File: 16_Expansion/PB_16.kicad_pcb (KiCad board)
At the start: 2 copper layers, 139.5 x 71 mm, 56 parts, among them J1 String1, J10 String10, J11 String11, J12 String12, J13 String13, J14 String14, J15 String15, J16 String16, J17 Power In Left, J18 Power In Right, J19 Expansion Header, J2 String2, J3 String3, J4 String4, J5 String5, J6 String6, J7 String7, J8 String8, J9 String9, U1 SN74HCT245N, U2 SN74HCT245N

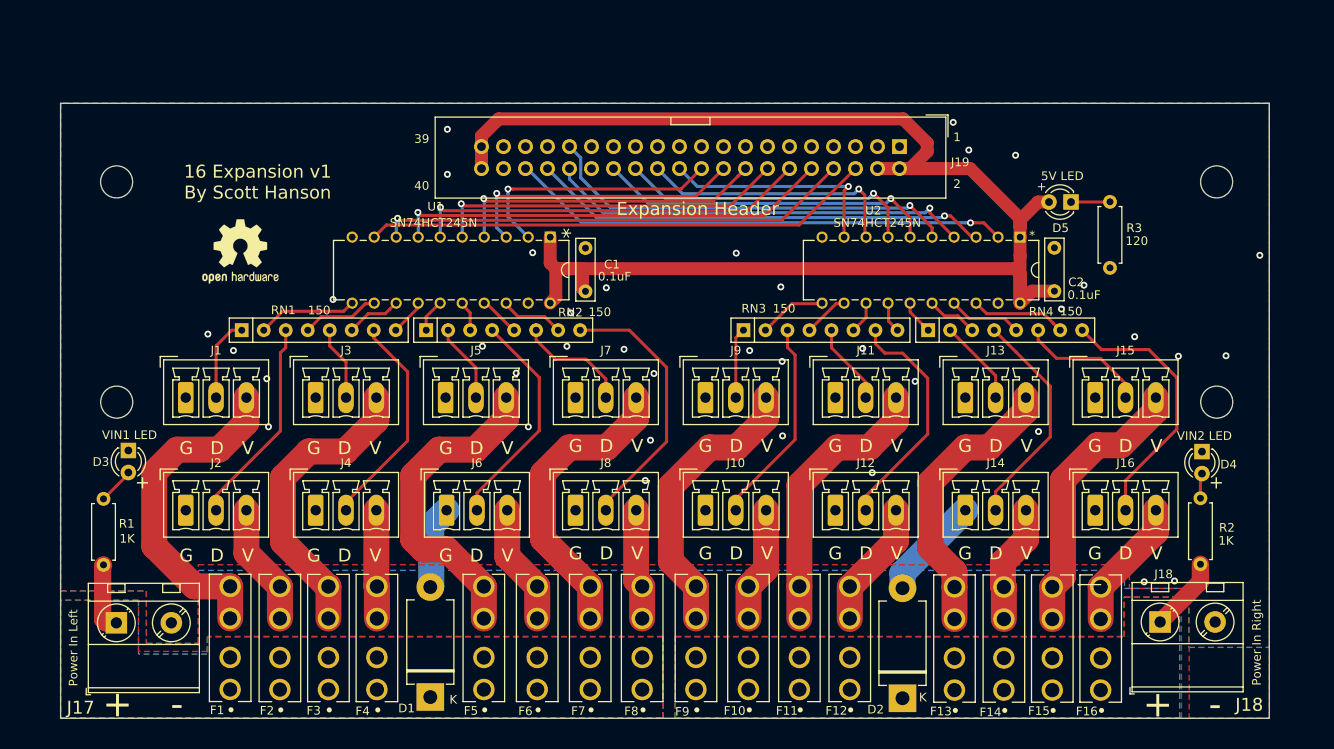
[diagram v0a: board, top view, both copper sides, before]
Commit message: added port number silk screen and moved LEDs a little
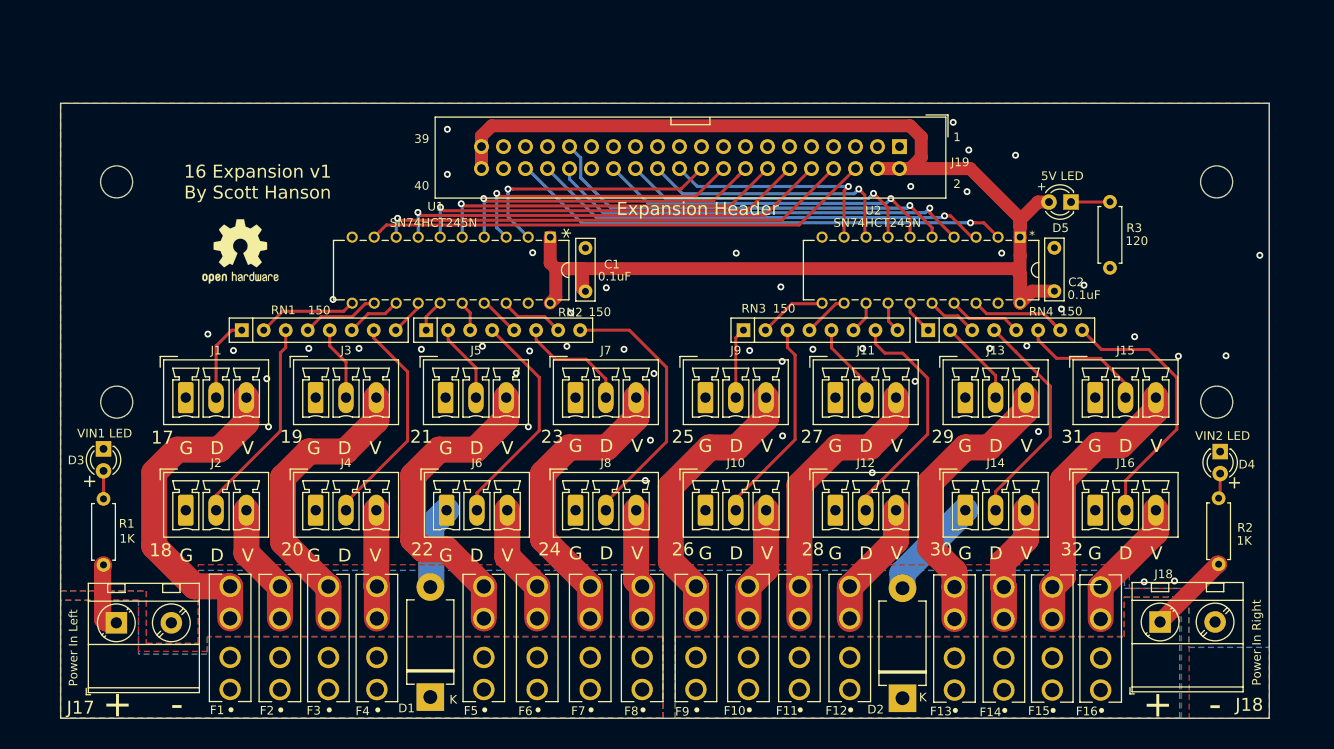
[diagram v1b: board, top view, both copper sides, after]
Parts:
- moved D3 2.88 mm to (79.6, 122.5)
- moved D4 2.10 mm to (208.5, 122.8)
- moved R2 2.10 mm to (208.3, 128.2)
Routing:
- net Net-(D3-Pad2): track 4.85 -> 3.23 mm
- net +5V: track 172.4 -> 171.1 mm
- net VIN2: track 8.85 -> 9.77 mm
- net GND: vias 38 -> 48
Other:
- board text added: "17"
- board text added: "18"
- board text added: "19"
- board text added: "20"
- board text added: "21"
- board text added: "22"
- board text added: "23"
- board text added: "24"
- board text added: "25"
- board text added: "26"
- board text added: "27"
- board text added: "28"
- board text added: "29"
- board text added: "30"
- board text added: "31"
- board text added: "32"

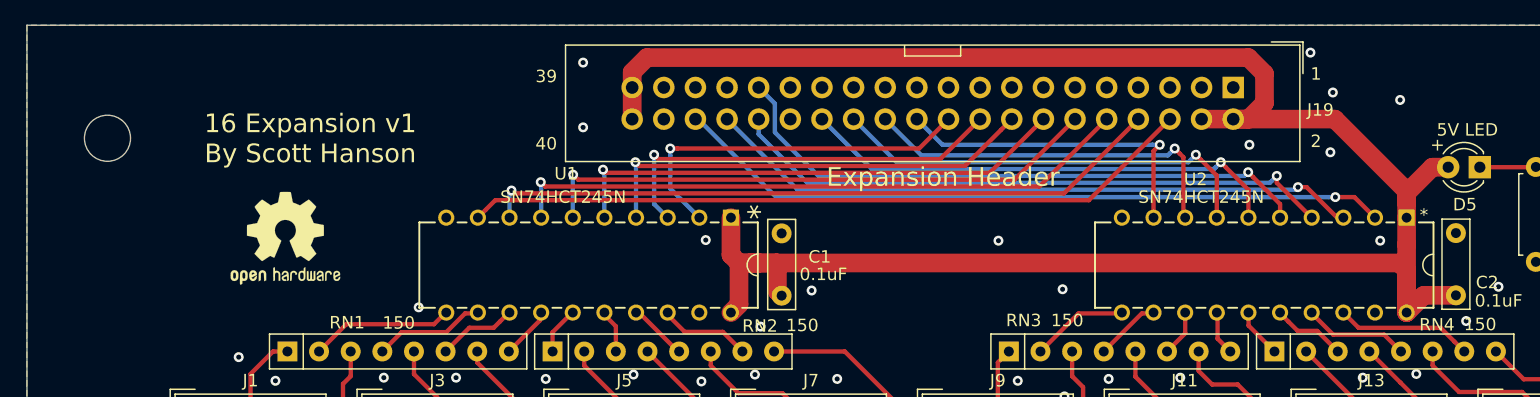
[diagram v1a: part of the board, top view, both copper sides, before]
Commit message: added Kicad logo
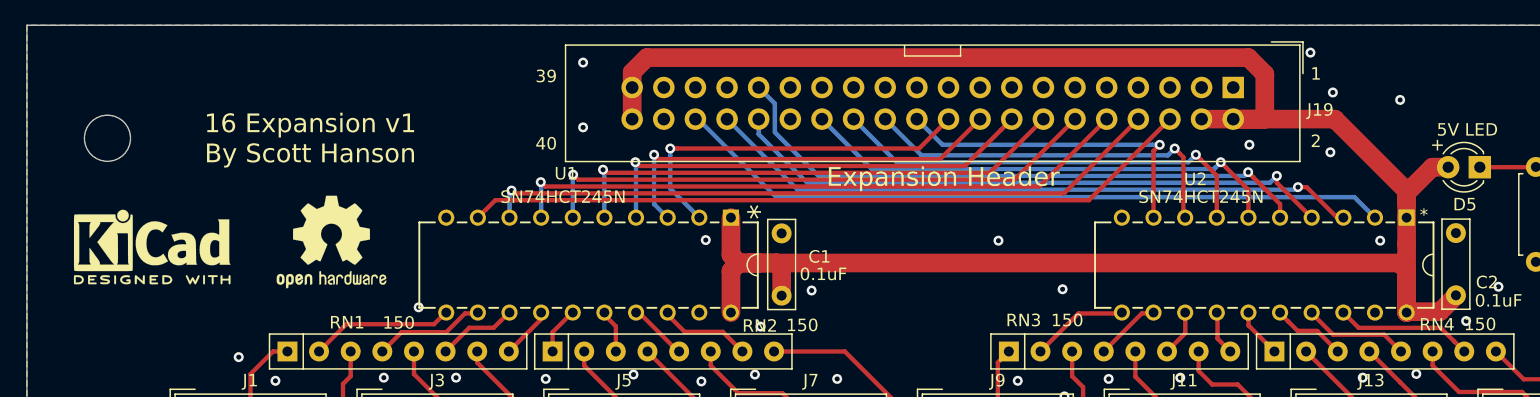
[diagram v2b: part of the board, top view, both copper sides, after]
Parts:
- added REF**: KiCad-Logo2_5mm_SilkScreen, Symbol:KiCad-Logo2_5mm_SilkScreen, F.Cu at (84.7, 100.4)
- moved REF** 3.71 mm to (99.1, 100.0)
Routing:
- net +5V: track 171.1 -> 172.0 mm
- net OUT32: vias 1 -> 0

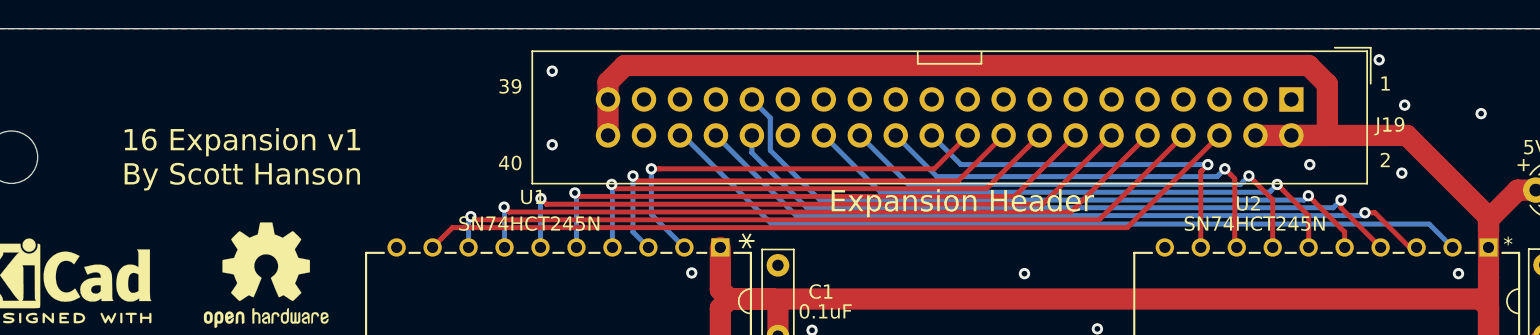
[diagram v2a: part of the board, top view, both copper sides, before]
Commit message: spun header around
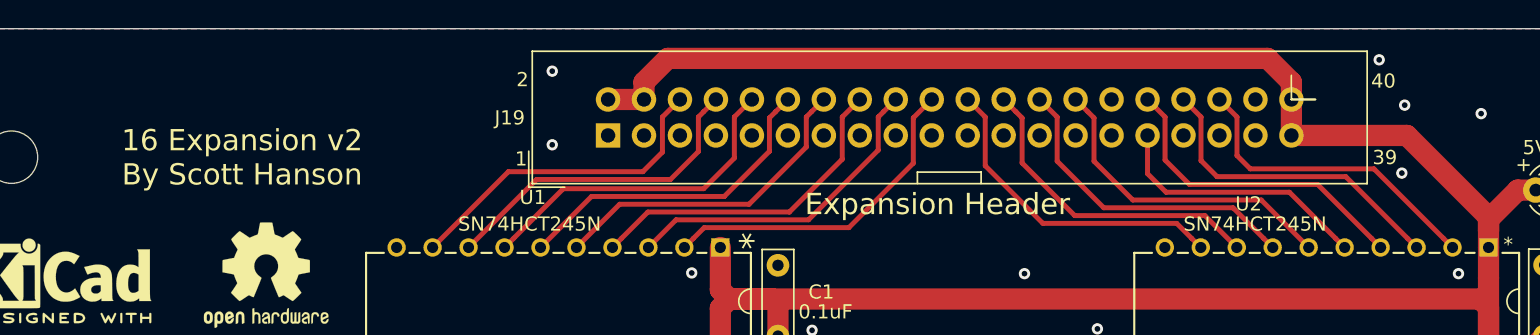
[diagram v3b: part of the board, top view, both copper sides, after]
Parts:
- moved J19 48.3 mm to (123.2, 90.2), turned to 90 degrees
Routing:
- net OUT17: track 58.8 -> 23.3 mm
- net OUT32: track 57.8 -> 22.4 mm
- net OUT18: track 55.1 -> 23.2 mm, vias 1 -> 0
- net OUT31: track 52.9 -> 23.1 mm, vias 1 -> 0
- net OUT29: track 48.4 -> 18.8 mm, vias 1 -> 0
- net OUT19: track 50.7 -> 23.5 mm, vias 1 -> 0
- net OUT30: track 49.2 -> 22.6 mm, vias 1 -> 0
- net OUT20: track 45.9 -> 23.2 mm, vias 1 -> 0
- net OUT21: track 41.1 -> 23.0 mm, vias 1 -> 0
- net OUT28: track 39.3 -> 22.6 mm, vias 1 -> 0
- net OUT22: track 36.4 -> 23.5 mm, vias 1 -> 0
- net OUT27: track 34.9 -> 22.6 mm, vias 1 -> 0
- net OUT23: track 33.2 -> 23.2 mm, vias 1 -> 0
- net +5V: track 172.0 -> 162.3 mm
- net OUT26: track 30.4 -> 22.7 mm, vias 1 -> 0
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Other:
- net class Gnd: clearance 0.3 -> 0.2
- board text added: "16 Expansion v2 By Scott Hanson"
- board text removed: "16 Expansion v1 By Scott Hanson"

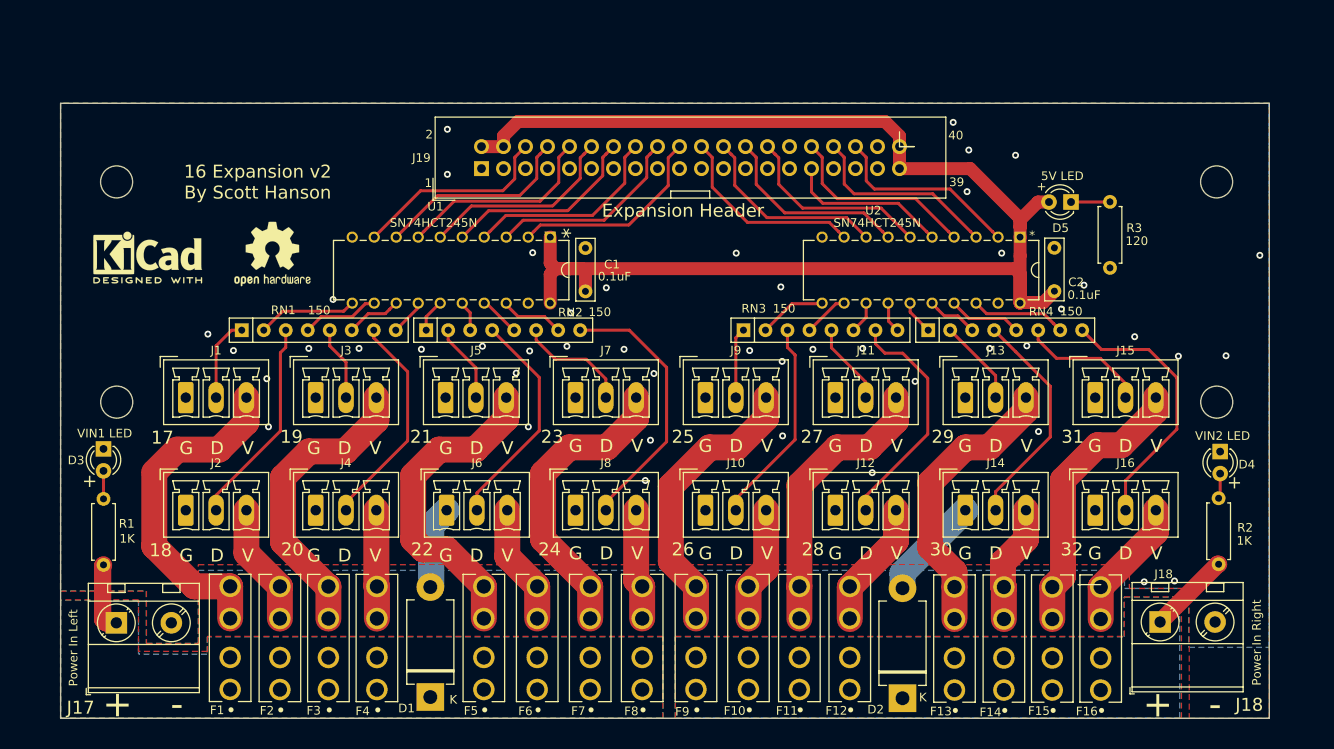
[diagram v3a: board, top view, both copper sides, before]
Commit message: switched 16 port expansion to screw terminals
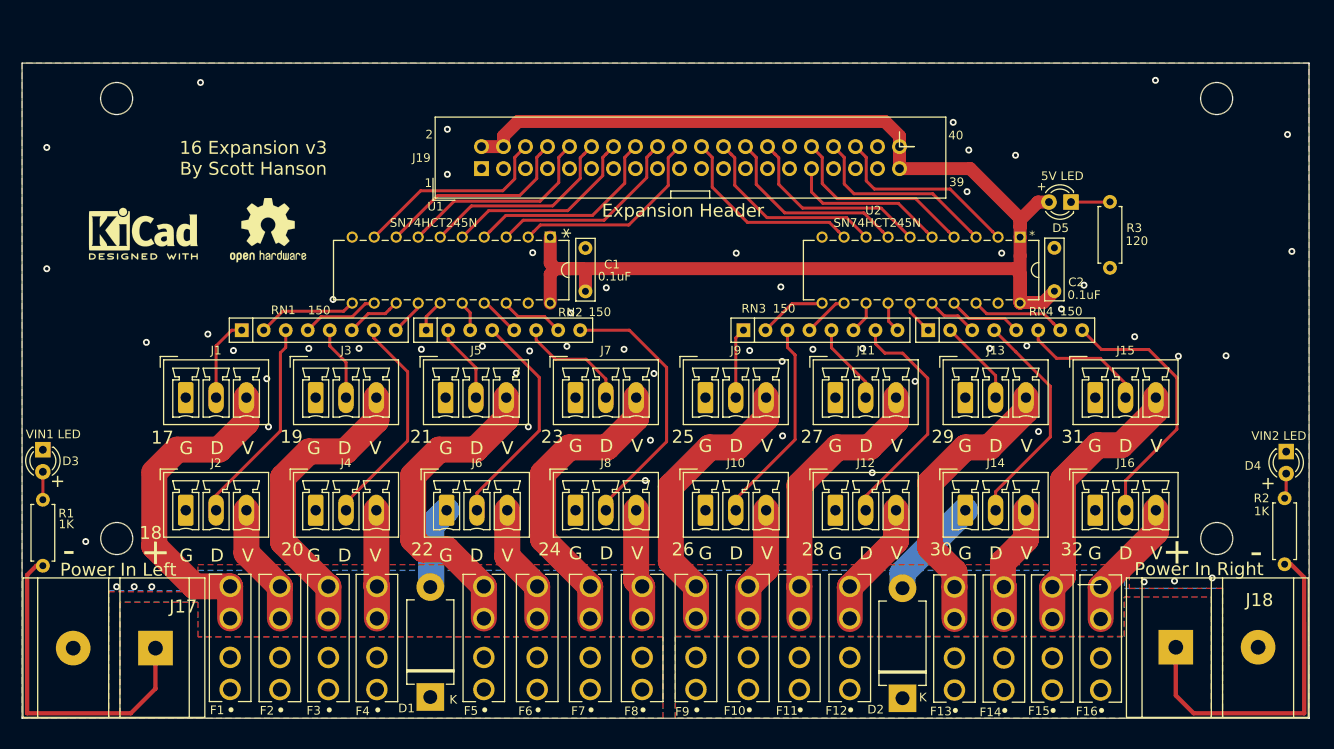
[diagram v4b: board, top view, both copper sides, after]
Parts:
- removed the REF** at (81.1, 117.1)
- removed the REF** at (208.1, 117.1)
- added REF**: MountingHole_3.7mm, MountingHole:MountingHole_3.7mm, F.Cu at (208.1, 132.9)
- added REF**: MountingHole_3.7mm, MountingHole:MountingHole_3.7mm, F.Cu at (81.1, 132.9)
- J17, J18: footprint TerminalBlock_MetzConnect:TerminalBlock_MetzConnect_Type701_RT11L02HGLU_1x02_P6.35mm_Horizontal -> Barrier_Blocks:BARRIER_BLOCK_1ROW_2POS_P9.5MM
- moved J18 11.7 mm to (197.7, 153.5)
- moved J17 11.5 mm to (91.3, 137.4), turned to 180 degrees
- moved REF** 9.63 mm to (81.1, 82.1)
- moved REF** 9.63 mm to (208.1, 82.1)
- moved D4 7.62 mm to (216.1, 122.8)
- moved R2 7.62 mm to (216.0, 128.2)
- moved D3 7.00 mm to (72.6, 122.6)
- moved R1 7.00 mm to (72.6, 128.4)
- moved REF** 2.80 mm to (84.2, 97.7)
- moved REF** 2.80 mm to (98.6, 97.3)
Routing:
- net VIN1: track 8.09 -> 38.9 mm
- net VIN2: track 9.77 -> 39.8 mm
- net GND: vias 47 -> 58
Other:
- board size 139.5 x 71 mm -> 148.6 x 75.6 mm
- net class Vin: trace_width 2 -> 0.5
- board text added: "16 Expansion v3 By Scott Hanson"
- board text removed: "16 Expansion v2 By Scott Hanson"

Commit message: aligned LED better
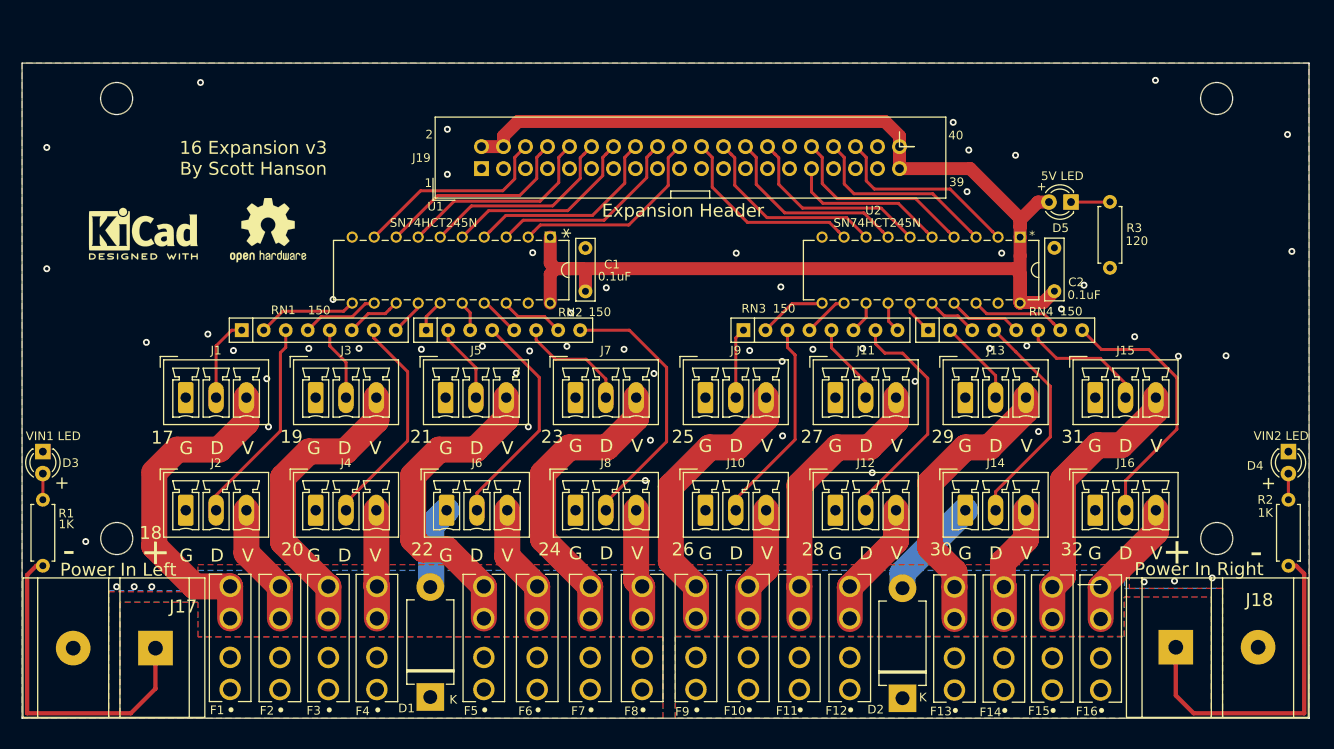
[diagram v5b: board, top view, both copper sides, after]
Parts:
- moved R2 0.47 mm to (216.4, 128.4)
- moved D4 0.26 mm to (216.4, 122.8)
- moved D3 0.21 mm to (72.6, 122.8)
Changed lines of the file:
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@@
     (thickness 1.6)
     (drawings 91)
-    (tracks 419)
+    (tracks 417)
     (zones 0)
     (modules 57)
@@
   )
   (module LED_THT:LED_D3.0mm_Clear (layer F.Cu)
-    (at 216.1422 122.831 270)
+    (at 216.401 122.831 270)
     (descr "IR-LED, diameter 3.0mm, 2 pins, color: clear")
     (tags "IR infrared LED diameter 3.0mm 2 pins clear")
@@
   )
   (module LED_THT:LED_D3.0mm_Clear (layer F.Cu)
-    (at 72.601 122.6178 270)
+    (at 72.601 122.831 270)
     (descr "IR-LED, diameter 3.0mm, 2 pins, color: clear")
     (tags "IR infrared LED diameter 3.0mm 2 pins clear")
@@
   )
   (module Resistor_THT:R_Axial_DIN0207_L6.3mm_D2.5mm_P7.62mm_Horizontal (layer F.Cu)
-    (at 215.9644 128.2158 270)
+    (at 216.401 128.392 270)
     (descr "Resistor, Axial_DIN0207 series, Axial, Horizontal, pin pitch=7.62mm, 0.25W = 1/4W, length*diameter=6.3*2.5mm^2, http://cdn-reichelt.de/documents/datenblatt/B400/1_4W%23YAG.pdf")
     (tags "Resistor Axial_DIN0207 series Axial Horizontal pin pitch 7.62mm 0.25W = 1/4W length 6.3mm diameter 2.5mm")
@@
   (gr_line (start 149.5894 92.747) (end 145.0894 92.747) (layer F.SilkS) (width 0.12))
   (gr_line (start 149.5894 93.547) (end 149.5894 92.747) (layer F.SilkS) (width 0.12))
-  (gr_text + (at 74.301 126.2178) (layer F.SilkS)
+  (gr_text + (at 74.801 126.4178) (layer F.SilkS)
     (effects (font (size 1.5 1.5) (thickness 0.3)))
   )
-  (gr_text + (at 214.051 126.4678) (layer F.SilkS)
+  (gr_text + (at 214.101 126.4678) (layer F.SilkS)
     (effects (font (size 1.5 1.5) (thickness 0.3)))
   )
@@
   (segment (start 130.35 125.35) (end 130.35 132.956) (width 3) (layer F.Cu) (net 18))
   (segment (start 203.401 150.9898) (end 203.401 145.4178) (width 0.5) (layer F.Cu) (net 19))
-  (segment (start 216.695 135.8358) (end 218.221693 137.362493) (width 0.5) (layer F.Cu) (net 19))
-  (segment (start 218.221693 137.362493) (end 218.225838 153.042776) (width 0.5) (layer F.Cu) (net 19))
-  (segment (start 218.225838 153.042776) (end 205.453811 153.042611) (width 0.5) (layer F.Cu) (net 19))
+  (segment (start 217.2952 136.012) (end 218.221581 136.938381) (width 0.5) (layer F.Cu) (net 19))
+  (segment (start 216.401 136.012) (end 217.2952 136.012) (width 0.5) (layer F.Cu) (net 19))
   (segment (start 205.453811 153.042611) (end 203.401 150.9898) (width 0.5) (layer F.Cu) (net 19))
-  (segment (start 215.9644 135.8358) (end 216.695 135.8358) (width 0.5) (layer F.Cu) (net 19))
+  (segment (start 218.221581 136.938381) (end 218.225838 153.042776) (width 0.5) (layer F.Cu) (net 19))
+  (segment (start 218.225838 153.042776) (end 205.453811 153.042611) (width 0.5) (layer F.Cu) (net 19))
   (segment (start 141.1 137.7055) (end 141.7931 138.3986) (width 3) (layer F.Cu) (net 20))
   (segment (start 141.1 129.6) (end 141.1 137.7055) (width 3) (layer F.Cu) (net 20))
@@
   (segment (start 169.371844 94.717844) (end 160.301044 94.717844) (width 0.35) (layer F.Cu) (net 68))
   (segment (start 172.7226 98.0686) (end 169.371844 94.717844) (width 0.35) (layer F.Cu) (net 68))
-  (segment (start 72.601 128.392) (end 72.601 125.1578) (width 0.35) (layer F.Cu) (net 69))
-  (segment (start 215.9644 125.5488) (end 216.1422 125.371) (width 0.35) (layer F.Cu) (net 70))
-  (segment (start 216.1422 128.038) (end 215.9644 128.2158) (width 0.35) (layer F.Cu) (net 70))
-  (segment (start 216.1422 125.371) (end 216.1422 128.038) (width 0.35) (layer F.Cu) (net 70))
+  (segment (start 72.601 125.371) (end 72.601 128.392) (width 0.35) (layer F.Cu) (net 69))
+  (segment (start 216.401 128.392) (end 216.401 125.371) (width 0.35) (layer F.Cu) (net 70))
   (segment (start 195.781 94.0178) (end 191.301 94.0178) (width 0.35) (layer F.Cu) (net 71))
   (segment (start 195.801 93.9978) (end 195.781 94.0178) (width 0.35) (layer F.Cu) (net 71))
